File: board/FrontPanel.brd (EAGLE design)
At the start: 76.2 x 44.5 mm, 10 parts, among them J1 PINHD-1X2BIG

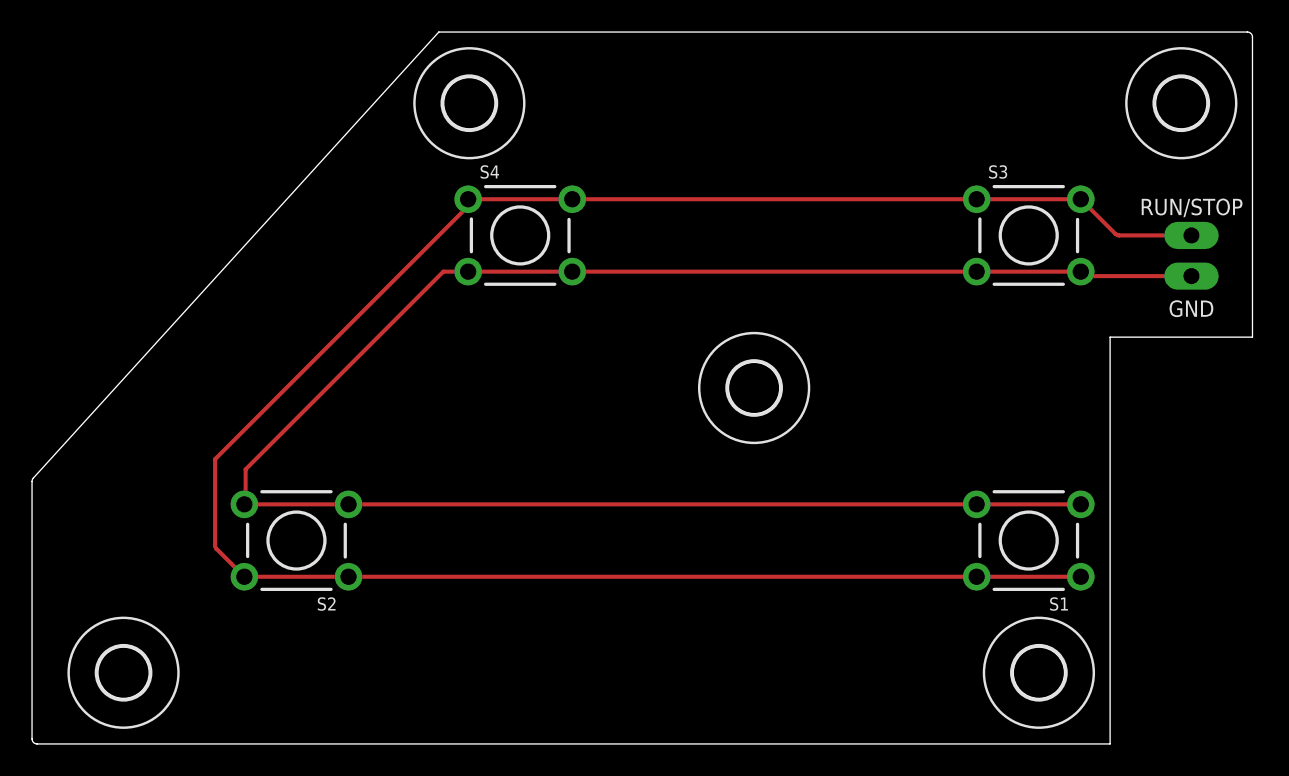
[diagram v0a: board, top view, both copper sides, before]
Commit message: Clean up front panel
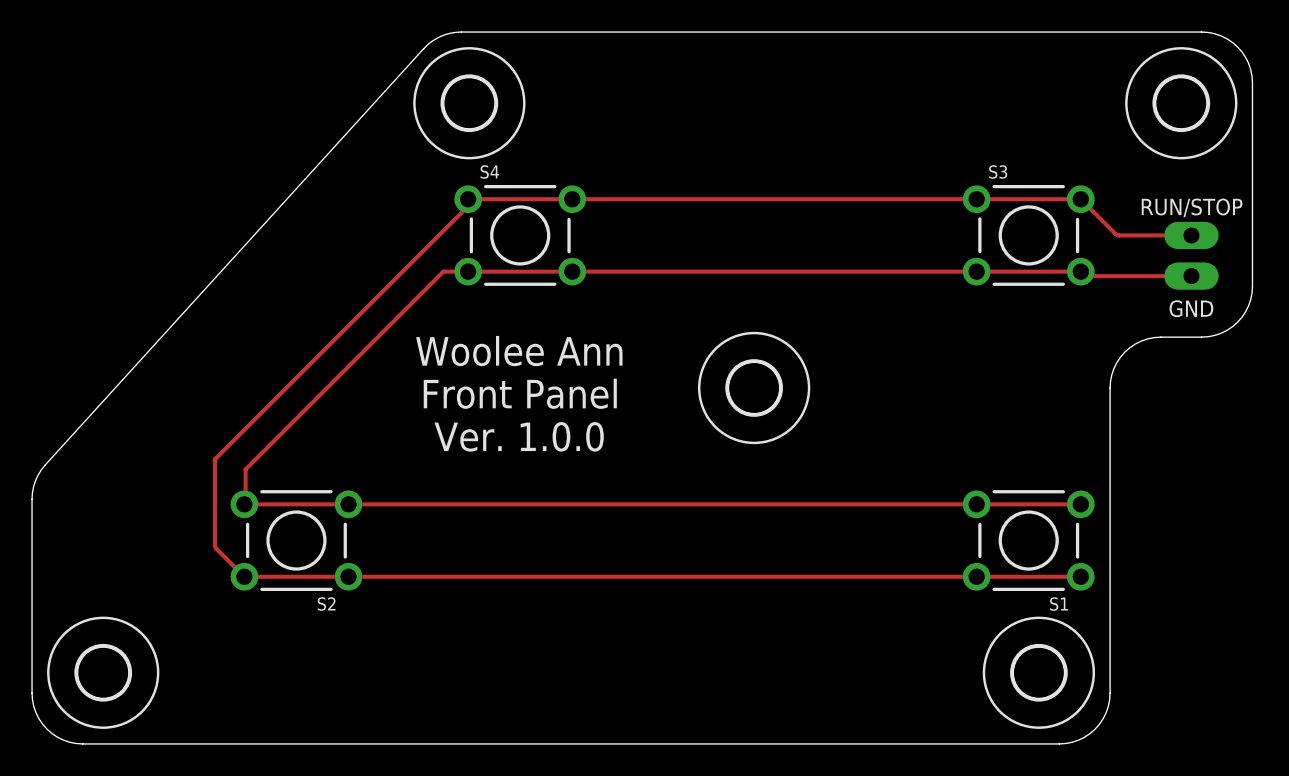
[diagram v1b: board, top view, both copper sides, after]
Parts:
- moved U$1 1.27 mm to (4.45, 4.45)
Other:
- outline, holes or cut-outs redrawn
- board text added: "Woolee Ann Front Panel Ver. 1.0.0"
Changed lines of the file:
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@@
 <board>
 <plain>
-<wire x1="0" y1="16.387253125" x2="0" y2="0.3175" width="0" layer="20"/>
-<wire x1="0" y1="0.3175" x2="0.3175" y2="0" width="0" layer="20" curve="90"/>
-<wire x1="0.3175" y1="0" x2="67.31" y2="0" width="0" layer="20"/>
-<wire x1="67.31" y1="0" x2="67.31" y2="25.4" width="0" layer="20"/>
-<wire x1="67.31" y1="25.4" x2="76.2" y2="25.4" width="0" layer="20"/>
-<wire x1="76.2" y1="25.4" x2="76.2" y2="44.1325" width="0" layer="20"/>
-<wire x1="76.2" y1="44.1325" x2="75.8825" y2="44.45" width="0" layer="20" curve="90"/>
-<wire x1="75.8825" y1="44.45" x2="25.4" y2="44.45" width="0" layer="20"/>
-<wire x1="25.4" y1="44.45" x2="0.08256875" y2="16.600825" width="0" layer="20"/>
-<wire x1="0.08256875" y1="16.600825" x2="0" y2="16.387253125" width="0" layer="20" curve="42.273277"/>
-<polygon width="0" layer="51" spacing="2.54" pour="hatch">
-<vertex x="6.35" y="15.24" curve="90"/>
-<vertex x="12.7" y="7.62"/>
-<vertex x="63.5" y="7.62" curve="90"/>
-<vertex x="69.85" y="13.97"/>
-<vertex x="69.85" y="30.48" curve="90"/>
-<vertex x="63.5" y="36.83"/>
-<vertex x="25.4" y="36.83" curve="0.903712"/>
-</polygon>
-<dimension x1="0" y1="0" x2="76.2" y2="0" x3="38.1" y3="-3.81" textsize="1.778" layer="51" unit="inch"/>
-<dimension x1="0" y1="0" x2="0" y2="16.51" x3="-2.54" y3="8.255" textsize="1.778" layer="51" unit="inch"/>
-<dimension x1="25.4" y1="44.45" x2="76.2" y2="44.45" x3="50.8" y3="46.99" textsize="1.778" layer="51" unit="inch"/>
-<dimension x1="76.2" y1="44.45" x2="76.2" y2="0" x3="83.82" y3="22.225" textsize="1.778" layer="51" unit="inch"/>
-<dimension x1="76.2" y1="25.4" x2="67.31" y2="25.4" x3="71.755" y3="21.59" textsize="1.778" layer="51" unit="inch"/>
-<dimension x1="67.31" y1="0" x2="67.31" y2="25.4" x3="78.74" y3="12.7" textsize="1.778" layer="51" unit="inch"/>
+<wire x1="76.2" y1="28.575" x2="76.2" y2="41.275" width="0" layer="20"/>
+<wire x1="76.2" y1="41.275" x2="73.025" y2="44.45" width="0" layer="20" curve="90"/>
+<wire x1="73.025" y1="44.45" x2="26.804525" y2="44.45" width="0" layer="20"/>
+<wire x1="26.804525" y1="44.45" x2="24.455215625" y2="43.4107375" width="0" layer="20" curve="47.726288"/>
+<wire x1="24.455215625" y1="43.4107375" x2="0.825690625" y2="17.418259375" width="0" layer="20"/>
+<wire x1="0.825690625" y1="17.418259375" x2="0" y2="15.282521875" width="0" layer="20" curve="42.273726"/>
+<wire x1="0" y1="15.282521875" x2="0" y2="3.175" width="0" layer="20"/>
+<wire x1="0" y1="3.175" x2="3.175" y2="0" width="0" layer="20" curve="90"/>
+<wire x1="3.175" y1="0" x2="64.135" y2="0" width="0" layer="20"/>
+<wire x1="64.135" y1="0" x2="67.31" y2="3.175" width="0" layer="20" curve="90"/>
+<wire x1="67.31" y1="3.175" x2="67.31" y2="22.225" width="0" layer="20"/>
+<wire x1="67.31" y1="22.225" x2="70.485" y2="25.4" width="0" layer="20" curve="-90"/>
+<wire x1="70.485" y1="25.4" x2="73.025" y2="25.4" width="0" layer="20"/>
+<wire x1="73.025" y1="25.4" x2="76.2" y2="28.575" width="0" layer="20" curve="90"/>
 <text x="72.39" y="33.02" size="1.016" layer="121" align="bottom-center">RUN/STOP</text>
 <text x="72.39" y="26.67" size="1.016" layer="121" align="bottom-center">GND</text>
+<text x="30.48" y="25.4" size="1.778" layer="121" align="top-center">Woolee Ann
+Front Panel
+Ver. 1.0.0</text>
 </plain>
 <attributes>
@@
 <element name="S4" library="SaintGimp" package="TACTILE-SWITCH-6MM" value="SWITCH-MOMENTARY-6MM" x="30.48" y="31.75"/>
 <element name="J1" library="SaintGimp" package="1X02-BIG" value="PINHD-1X2BIG" x="72.39" y="30.48" smashed="yes" rot="R270"/>
-<element name="U$1" library="holes" package="3,2" value="" x="5.715" y="4.445"/>
+<element name="U$1" library="holes" package="3,2" value="" x="4.445" y="4.445"/>
 <element name="U$2" library="holes" package="3,2" value="" x="62.865" y="4.445"/>
 <element name="U$3" library="holes" package="3,2" value="" x="27.305" y="40.005"/>
@@
 </board>
 </drawing>
+<compatibility>
+<note version="6.3" minversion="6.2.2" severity="warning">
+Since Version 6.2.2 text objects can contain more than one line,
+which will not be processed correctly with this version.
+</note>
+</compatibility>
 </eagle>

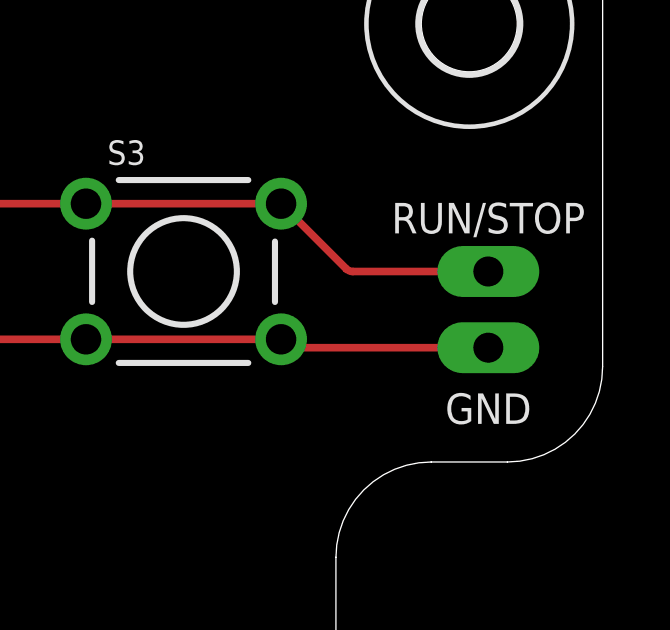
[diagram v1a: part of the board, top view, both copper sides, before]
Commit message: Front panel tweaks
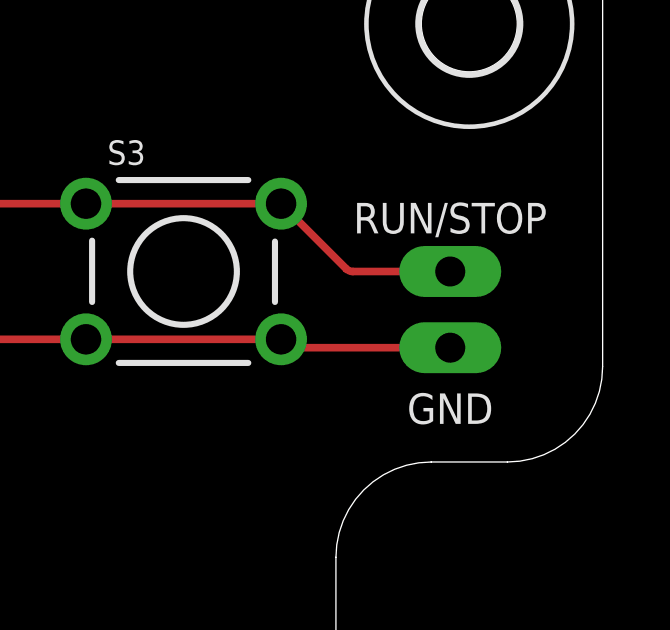
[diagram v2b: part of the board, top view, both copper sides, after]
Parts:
- moved J1 1.27 mm to (71.1, 30.5)
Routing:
- net N$2: track 118.7 -> 117.4 mm
- net N$1: track 129.1 -> 127.9 mm
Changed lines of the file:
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@@
 <wire x1="70.485" y1="25.4" x2="73.025" y2="25.4" width="0" layer="20"/>
 <wire x1="73.025" y1="25.4" x2="76.2" y2="28.575" width="0" layer="20" curve="90"/>
-<text x="72.39" y="33.02" size="1.016" layer="121" align="bottom-center">RUN/STOP</text>
-<text x="72.39" y="26.67" size="1.016" layer="121" align="bottom-center">GND</text>
+<text x="71.12" y="33.02" size="1.016" layer="121" align="bottom-center">RUN/STOP</text>
+<text x="71.12" y="26.67" size="1.016" layer="121" align="bottom-center">GND</text>
 <text x="30.48" y="25.4" size="1.778" layer="121" align="top-center">Woolee Ann
 Front Panel
@@
 <element name="S3" library="SaintGimp" package="TACTILE-SWITCH-6MM" value="SWITCH-MOMENTARY-6MM" x="62.23" y="31.75"/>
 <element name="S4" library="SaintGimp" package="TACTILE-SWITCH-6MM" value="SWITCH-MOMENTARY-6MM" x="30.48" y="31.75"/>
-<element name="J1" library="SaintGimp" package="1X02-BIG" value="PINHD-1X2BIG" x="72.39" y="30.48" smashed="yes" rot="R270"/>
+<element name="J1" library="SaintGimp" package="1X02-BIG" value="PINHD-1X2BIG" x="71.12" y="30.48" smashed="yes" rot="R270"/>
 <element name="U$1" library="holes" package="3,2" value="" x="4.445" y="4.445"/>
 <element name="U$2" library="holes" package="3,2" value="" x="62.865" y="4.445"/>
@@
 <contactref element="S4" pad="1"/>
 <contactref element="S4" pad="2"/>
-<wire x1="72.39" y1="31.75" x2="67.8733125" y2="31.75" width="0.254" layer="1"/>
+<wire x1="71.12" y1="31.75" x2="67.8733125" y2="31.75" width="0.254" layer="1"/>
 <wire x1="67.8733125" y1="31.75" x2="67.64880625" y2="31.84299375" width="0.254" layer="1" curve="-45"/>
 <wire x1="67.64880625" y1="31.84299375" x2="65.4812" y2="34.0106" width="0.254" layer="1"/>
@@
 <contactref element="S1" pad="3"/>
 <contactref element="J1" pad="2"/>
-<wire x1="72.39" y1="29.21" x2="65.8921125" y2="29.21" width="0.254" layer="1"/>
+<wire x1="71.12" y1="29.21" x2="65.8921125" y2="29.21" width="0.254" layer="1"/>
 <wire x1="65.8921125" y1="29.21" x2="65.66760625" y2="29.30299375" width="0.254" layer="1" curve="-45"/>
 <wire x1="65.66760625" y1="29.30299375" x2="65.4812" y2="29.4894" width="0.254" layer="1"/>
